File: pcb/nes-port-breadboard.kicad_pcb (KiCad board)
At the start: 2 copper layers, 35.6 x 35.6 mm, 4 parts, among them J1 NES_Port_Male, J2 Conn_01x07

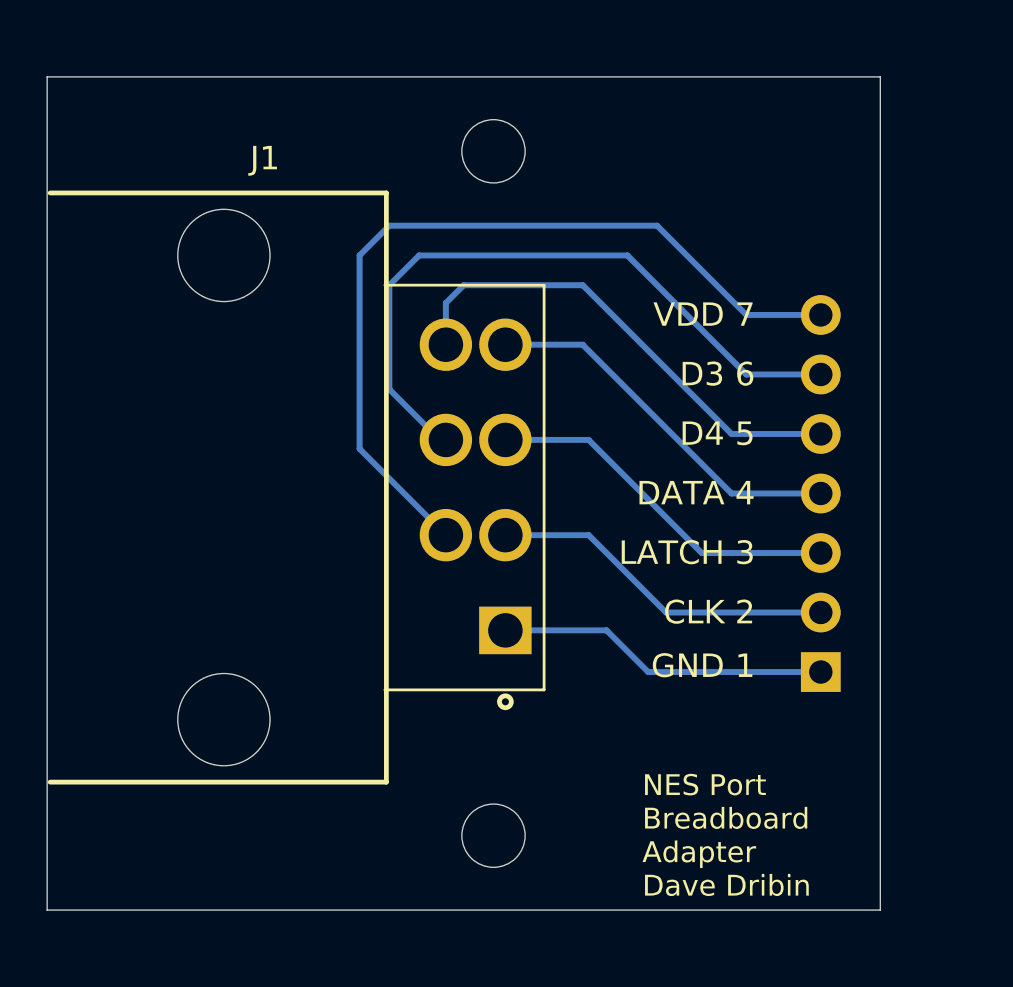
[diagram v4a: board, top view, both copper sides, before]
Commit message: Tweak footprint og NES port
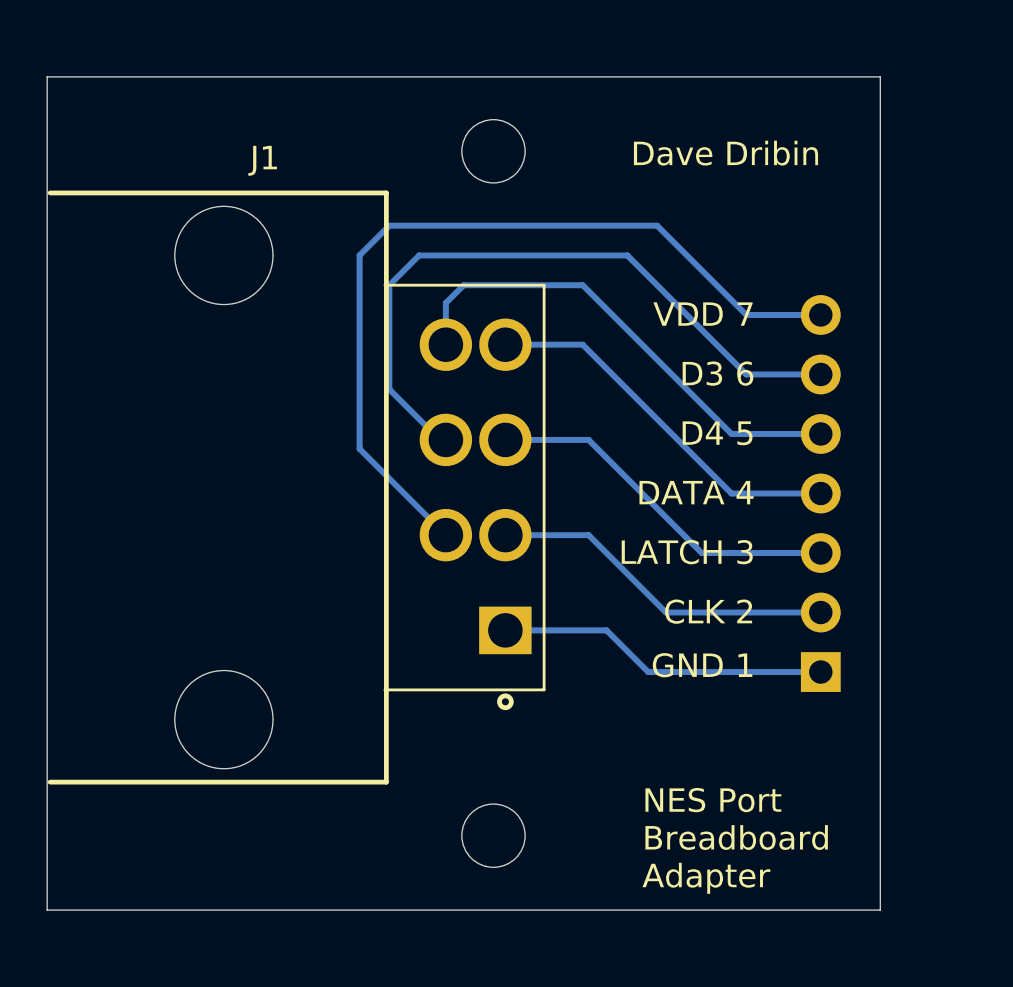
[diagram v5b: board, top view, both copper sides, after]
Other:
- board text added: "Dave Dribin"
- board text added: "NES Port Breadboard Adapter"
- board text removed: "NES Port Breadboard Adapter Dave Dribin"
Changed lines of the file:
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@@
   (general
     (thickness 1.6)
-    (drawings 18)
+    (drawings 19)
     (tracks 30)
     (zones 0)
@@
     (mod_text_size 1 1)
     (mod_text_width 0.15)
-    (pad_size 1.524 1.524)
-    (pad_drill 0.762)
+    (pad_size 4.191 4.191)
+    (pad_drill 4.191)
     (pad_to_mask_clearance 0.0508)
     (aux_axis_origin 0 0)
@@
       (effects (font (size 1 1) (thickness 0.15)))
     )
+    (fp_circle (center -1.016 9.144) (end -0.762 9.144) (layer F.SilkS) (width 0.2032))
+    (fp_line (start 0.635 8.636) (end -6.1595 8.636) (layer F.SilkS) (width 0.12))
+    (fp_line (start 0.635 -8.636) (end 0.635 8.636) (layer F.SilkS) (width 0.12))
+    (fp_line (start -6.1595 -8.636) (end 0.635 -8.636) (layer F.SilkS) (width 0.12))
+    (fp_line (start -6.096 12.573) (end -20.447 12.573) (layer F.SilkS) (width 0.2032))
+    (fp_line (start -6.096 -12.573) (end -6.096 12.573) (layer F.SilkS) (width 0.2032))
+    (fp_line (start 0 -8.001) (end 0 8.001) (layer F.Fab) (width 0.12))
+    (fp_line (start -6.223 8.001) (end 0 8.001) (layer F.Fab) (width 0.12))
+    (fp_line (start -6.223 -8.001) (end 0 -8.001) (layer F.Fab) (width 0.12))
+    (fp_line (start -6.2484 12.446) (end -20.4724 12.446) (layer F.Fab) (width 0.1016))
+    (fp_line (start -20.447 -12.573) (end -6.096 -12.573) (layer F.SilkS) (width 0.2032))
+    (fp_line (start -20.4724 -12.446) (end -20.4724 12.446) (layer F.Fab) (width 0.1016))
+    (fp_line (start -6.2484 -12.446) (end -6.2484 12.446) (layer F.Fab) (width 0.1016))
+    (fp_line (start -17.4752 -12.446) (end -17.4752 -14.859) (layer F.Fab) (width 0.1016))
+    (fp_line (start -17.4752 -14.859) (end -15.2146 -14.859) (layer F.Fab) (width 0.1016))
+    (fp_line (start -15.2146 -14.859) (end -15.2146 -12.446) (layer F.Fab) (width 0.1016))
+    (fp_line (start -15.2146 14.859) (end -15.2146 12.446) (layer F.Fab) (width 0.1016))
+    (fp_line (start -17.4752 12.446) (end -17.4752 14.859) (layer F.Fab) (width 0.1016))
+    (fp_line (start -17.4752 14.859) (end -15.2146 14.859) (layer F.Fab) (width 0.1016))
     (fp_line (start -20.4724 -12.446) (end -6.2484 -12.446) (layer F.Fab) (width 0.1016))
-    (fp_line (start -17.4752 14.859) (end -15.2146 14.859) (layer F.Fab) (width 0.1016))
-    (fp_line (start -17.4752 12.446) (end -17.4752 14.859) (layer F.Fab) (width 0.1016))
-    (fp_line (start -15.2146 14.859) (end -15.2146 12.446) (layer F.Fab) (width 0.1016))
-    (fp_line (start -15.2146 -14.859) (end -15.2146 -12.446) (layer F.Fab) (width 0.1016))
-    (fp_line (start -17.4752 -14.859) (end -15.2146 -14.859) (layer F.Fab) (width 0.1016))
-    (fp_line (start -17.4752 -12.446) (end -17.4752 -14.859) (layer F.Fab) (width 0.1016))
-    (fp_line (start -6.2484 -12.446) (end -6.2484 12.446) (layer F.Fab) (width 0.1016))
-    (fp_line (start -20.4724 -12.446) (end -20.4724 12.446) (layer F.Fab) (width 0.1016))
-    (fp_line (start -20.447 -12.573) (end -6.096 -12.573) (layer F.SilkS) (width 0.2032))
-    (fp_line (start -6.2484 12.446) (end -20.4724 12.446) (layer F.Fab) (width 0.1016))
-    (fp_line (start -6.223 -8.001) (end 0 -8.001) (layer F.Fab) (width 0.12))
-    (fp_line (start -6.223 8.001) (end 0 8.001) (layer F.Fab) (width 0.12))
-    (fp_line (start 0 -8.001) (end 0 8.001) (layer F.Fab) (width 0.12))
-    (fp_line (start -6.096 -12.573) (end -6.096 12.573) (layer F.SilkS) (width 0.2032))
-    (fp_line (start -6.096 12.573) (end -20.447 12.573) (layer F.SilkS) (width 0.2032))
-    (fp_line (start -6.1595 -8.636) (end 0.635 -8.636) (layer F.SilkS) (width 0.12))
-    (fp_line (start 0.635 -8.636) (end 0.635 8.636) (layer F.SilkS) (width 0.12))
-    (fp_line (start 0.635 8.636) (end -6.1595 8.636) (layer F.SilkS) (width 0.12))
-    (fp_circle (center -1.016 9.144) (end -0.762 9.144) (layer F.SilkS) (width 0.2032))
     (pad 4 thru_hole circle (at -1.016 -6.096) (size 2.2352 2.2352) (drill 1.4732) (layers *.Cu *.Mask)
       (net 4 "Net-(J1-Pad4)"))
@@
     (pad 6 thru_hole circle (at -3.556 -2.032) (size 2.2352 2.2352) (drill 1.4732) (layers *.Cu *.Mask)
       (net 6 "Net-(J1-Pad6)"))
-    (pad "" np_thru_hole circle (at -13.0302 -9.906) (size 3.937 3.937) (drill 3.937) (layers *.Cu *.Mask))
-    (pad "" np_thru_hole circle (at -13.0302 9.906) (size 3.937 3.937) (drill 3.937) (layers *.Cu *.Mask))
+    (pad "" np_thru_hole circle (at -13.0302 -9.906) (size 4.191 4.191) (drill 4.191) (layers *.Cu *.Mask))
+    (pad "" np_thru_hole circle (at -13.0302 9.906) (size 4.191 4.191) (drill 4.191) (layers *.Cu *.Mask))
   )
   (module Connector_PinHeader_2.54mm:PinHeader_1x07_P2.54mm_Vertical (layer B.Cu)
@@
       (effects (font (size 1 1) (thickness 0.15)) (justify mirror))
     )
+    (fp_line (start -0.635 1.27) (end 1.27 1.27) (layer B.Fab) (width 0.1))
+    (fp_line (start 1.27 1.27) (end 1.27 -16.51) (layer B.Fab) (width 0.1))
+    (fp_line (start 1.27 -16.51) (end -1.27 -16.51) (layer B.Fab) (width 0.1))
+    (fp_line (start -1.27 -16.51) (end -1.27 0.635) (layer B.Fab) (width 0.1))
+    (fp_line (start -1.27 0.635) (end -0.635 1.27) (layer B.Fab) (width 0.1))
+    (fp_line (start -1.33 -16.57) (end 1.33 -16.57) (layer B.SilkS) (width 0.12))
+    (fp_line (start -1.33 -1.27) (end -1.33 -16.57) (layer B.SilkS) (width 0.12))
+    (fp_line (start 1.33 -1.27) (end 1.33 -16.57) (layer B.SilkS) (width 0.12))
+    (fp_line (start -1.33 -1.27) (end 1.33 -1.27) (layer B.SilkS) (width 0.12))
+    (fp_line (start -1.33 0) (end -1.33 1.33) (layer B.SilkS) (width 0.12))
+    (fp_line (start -1.33 1.33) (end 0 1.33) (layer B.SilkS) (width 0.12))
+    (fp_line (start -1.8 1.8) (end -1.8 -17.05) (layer B.CrtYd) (width 0.05))
+    (fp_line (start -1.8 -17.05) (end 1.8 -17.05) (layer B.CrtYd) (width 0.05))
+    (fp_line (start 1.8 -17.05) (end 1.8 1.8) (layer B.CrtYd) (width 0.05))
     (fp_line (start 1.8 1.8) (end -1.8 1.8) (layer B.CrtYd) (width 0.05))
-    (fp_line (start 1.8 -17.05) (end 1.8 1.8) (layer B.CrtYd) (width 0.05))
-    (fp_line (start -1.8 -17.05) (end 1.8 -17.05) (layer B.CrtYd) (width 0.05))
-    (fp_line (start -1.8 1.8) (end -1.8 -17.05) (layer B.CrtYd) (width 0.05))
-    (fp_line (start -1.33 1.33) (end 0 1.33) (layer B.SilkS) (width 0.12))
-    (fp_line (start -1.33 0) (end -1.33 1.33) (layer B.SilkS) (width 0.12))
-    (fp_line (start -1.33 -1.27) (end 1.33 -1.27) (layer B.SilkS) (width 0.12))
-    (fp_line (start 1.33 -1.27) (end 1.33 -16.57) (layer B.SilkS) (width 0.12))
-    (fp_line (start -1.33 -1.27) (end -1.33 -16.57) (layer B.SilkS) (width 0.12))
-    (fp_line (start -1.33 -16.57) (end 1.33 -16.57) (layer B.SilkS) (width 0.12))
-    (fp_line (start -1.27 0.635) (end -0.635 1.27) (layer B.Fab) (width 0.1))
-    (fp_line (start -1.27 -16.51) (end -1.27 0.635) (layer B.Fab) (width 0.1))
-    (fp_line (start 1.27 -16.51) (end -1.27 -16.51) (layer B.Fab) (width 0.1))
-    (fp_line (start 1.27 1.27) (end 1.27 -16.51) (layer B.Fab) (width 0.1))
-    (fp_line (start -0.635 1.27) (end 1.27 1.27) (layer B.Fab) (width 0.1))
     (fp_text user %R (at 0 -7.62 270) (layer B.Fab)
       (effects (font (size 1 1) (thickness 0.15)) (justify mirror))
@@
       (effects (font (size 1 1) (thickness 0.15)))
     )
+    (fp_circle (center 0 0) (end 2.7 0) (layer Cmts.User) (width 0.15))
     (fp_circle (center 0 0) (end 2.95 0) (layer F.CrtYd) (width 0.05))
-    (fp_circle (center 0 0) (end 2.7 0) (layer Cmts.User) (width 0.15))
     (fp_text user %R (at 0.3 0) (layer F.Fab) hide
       (effects (font (size 1 1) (thickness 0.15)))
@@
       (effects (font (size 1 1) (thickness 0.15)))
     )
+    (fp_circle (center 0 0) (end 2.7 0) (layer Cmts.User) (width 0.15))
     (fp_circle (center 0 0) (end 2.95 0) (layer F.CrtYd) (width 0.05))
-    (fp_circle (center 0 0) (end 2.7 0) (layer Cmts.User) (width 0.15))
     (fp_text user %R (at 0.3 0) (layer F.Fab) hide
       (effects (font (size 1 1) (thickness 0.15)))
     )
     (pad 1 np_thru_hole circle (at 0 0) (size 2.7 2.7) (drill 2.7) (layers *.Cu *.Mask))
+  )
+  (gr_text "Dave Dribin" (at 160.02 93.472) (layer F.SilkS)
+    (effects (font (size 1 1) (thickness 0.15)) (justify right))
   )
   (gr_line (start 123.19 127) (end 123.19 127) (layer Edge.Cuts) (width 0.0254))
   (gr_text M2.5 (at 141.605 122.555) (layer B.SilkS)
-    (effects (font (size 0.762 0.762) (thickness 0.127)) (justify mirror))
+    (effects (font (size 1 1) (thickness 0.15)) (justify mirror))
   )
   (gr_text M2.5 (at 141.605 93.345) (layer B.SilkS)
-    (effects (font (size 0.762 0.762) (thickness 0.127)) (justify mirror))
+    (effects (font (size 1 1) (thickness 0.15)) (justify mirror))
   )
   (dimension 35.56 (width 0.15) (layer Dwgs.User)
@@
     (arrow2b (pts (xy 165.735 90.17) (xy 166.321421 91.296504)))
   )
-  (gr_text "Version 1.0.1" (at 160.02 93.345) (layer B.SilkS)
-    (effects (font (size 0.889 0.889) (thickness 0.09525)) (justify left mirror))
-  )
-  (gr_text "NES Port\nBreadboard\nAdapter\nDave Dribin" (at 152.4 122.555) (layer F.SilkS)
-    (effects (font (size 0.889 0.889) (thickness 0.15)) (justify left))
+  (gr_text "Version 1.0.1" (at 160.02 93.472) (layer B.SilkS)
+    (effects (font (size 1 1) (thickness 0.15)) (justify left mirror))
+  )
+  (gr_text "NES Port\nBreadboard\nAdapter" (at 152.4 122.682) (layer F.SilkS)
+    (effects (font (size 1 1) (thickness 0.15)) (justify left))
   )
   (gr_text "VDD 7" (at 157.226 100.33) (layer F.SilkS)
